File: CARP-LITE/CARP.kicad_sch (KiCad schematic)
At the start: 111 parts, among them J1 USB-C, J10 PYRO_2, J3 I2C1+3V3, J4 2S XT30, J5 UART+5V+I2C1, J6 PYRO_1, J8 PWM1+5V1, J9 PWM2+5V1, Q5 SQ2318CES, Q6 SQ2318CES, Q7 SQ2318CES, SW1 SW_Push, SW2 SW_Push, U1 W25Q128JVSIMTR (16MB), U10 TPS62130A, U2 W25Q32RVXHJQ (2MB), U3 3V3 LDO, U4 RP2350_60QFN, U5 LSM6DSO, U6 BMP390, Y1 ABM8-272-T3

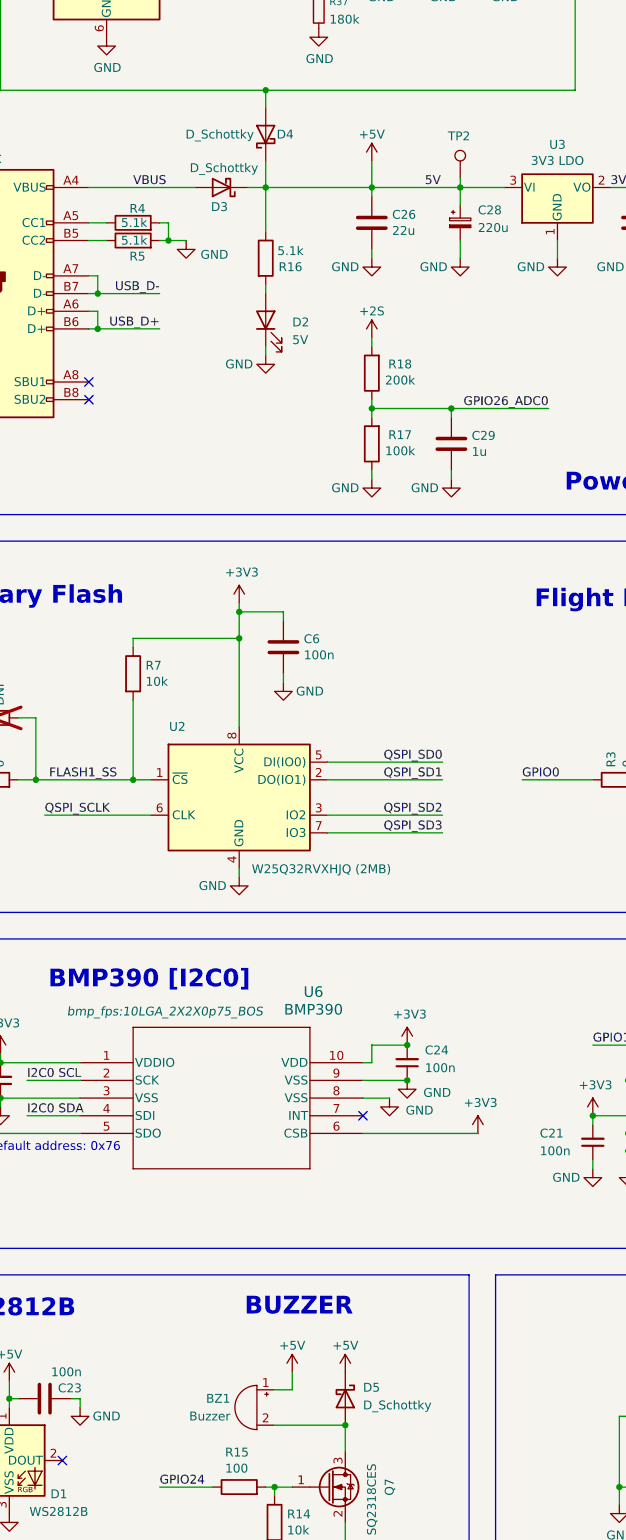
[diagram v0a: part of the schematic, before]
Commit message: Change passives footprints to 0603
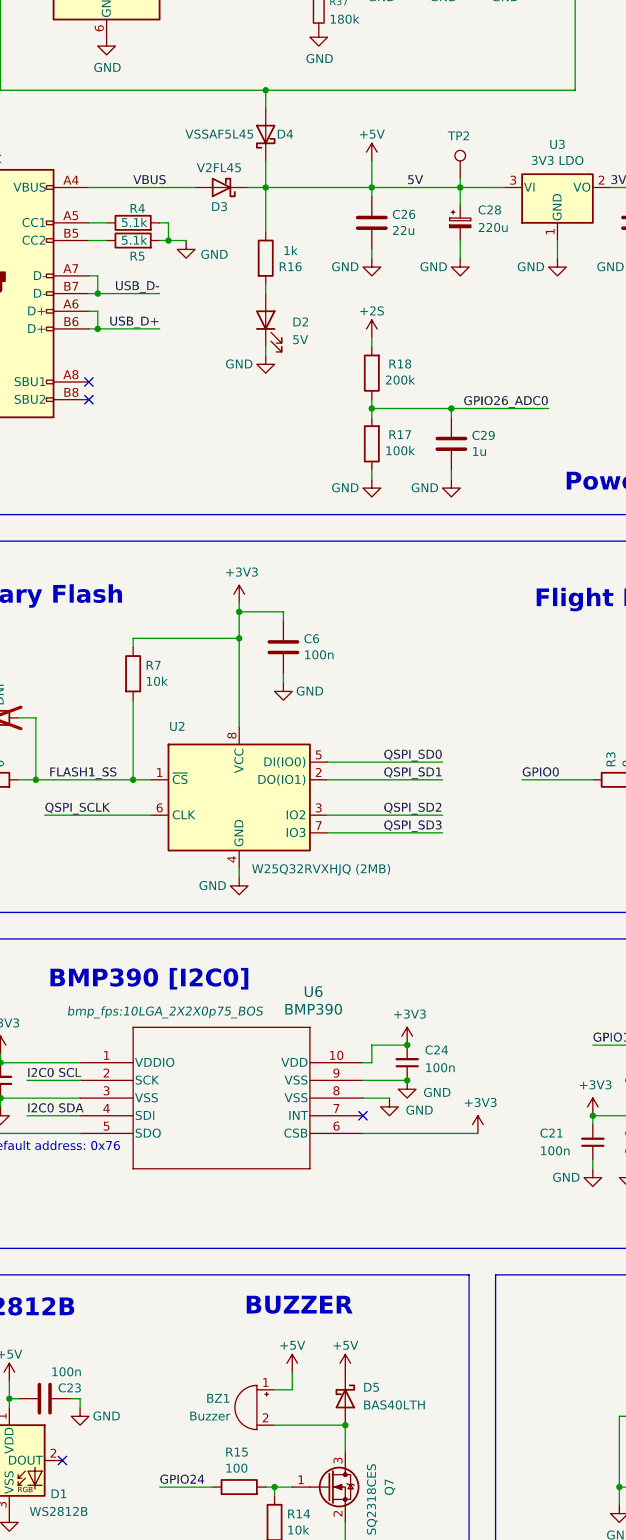
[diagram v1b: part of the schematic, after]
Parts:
- D3: value D_Schottky -> V2FL45
- D4: value D_Schottky -> VSSAF5L45
- D5: value D_Schottky -> BAS40LTH
- R16: value 5.1k -> 1k
- R19, R20, R21, R22, R24, R25, R26, R31, R32, R33, R34, R35, R4, R5, R8: footprint Resistor_SMD:R_0402_1005Metric -> Resistor_SMD:R_0603_1608Metric
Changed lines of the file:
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@@
 	)
 	(label "5V"
-		(at 93.98 81.28 0)
+		(at 91.44 81.28 0)
 		(effects
 			(font
@@
 			)
 		)
-		(property "Footprint" "Resistor_SMD:R_0402_1005Metric"
+		(property "Footprint" "Resistor_SMD:R_0603_1608Metric"
 			(at 328.93 239.268 90)
 			(hide yes)
@@
 			)
 		)
-		(property "Footprint" "Resistor_SMD:R_0402_1005Metric"
+		(property "Footprint" "Resistor_SMD:R_0603_1608Metric"
 			(at 168.148 55.88 90)
 			(hide yes)
@@
 			)
 		)
-		(property "Footprint" "Resistor_SMD:R_0402_1005Metric"
+		(property "Footprint" "Resistor_SMD:R_0603_1608Metric"
 			(at 52.07 88.138 90)
 			(hide yes)
@@
 			)
 		)
-		(property "Value" "5.1k"
+		(property "Value" "1k"
 			(at 74.676 90.3986 0)
 			(show_name no)
@@
 			)
 		)
-		(property "Footprint" "Resistor_SMD:R_0402_1005Metric"
+		(property "Footprint" "Resistor_SMD:R_0603_1608Metric"
 			(at 169.672 55.88 90)
 			(hide yes)
@@
 			)
 		)
-		(property "Footprint" "Resistor_SMD:R_0402_1005Metric"
+		(property "Footprint" "Resistor_SMD:R_0603_1608Metric"
 			(at 341.122 205.74 90)
 			(hide yes)
@@
 			)
 		)
-		(property "Value" "D_Schottky"
+		(property "Value" "BAS40LTH"
 			(at 85.09 256.2224 90)
 			(show_name no)
@@
 			)
 		)
-		(property "Footprint" "Resistor_SMD:R_0402_1005Metric"
+		(property "Footprint" "Resistor_SMD:R_0603_1608Metric"
 			(at 334.772 185.42 90)
 			(hide yes)
@@
 			)
 		)
-		(property "Footprint" "Resistor_SMD:R_0402_1005Metric"
+		(property "Footprint" "Resistor_SMD:R_0603_1608Metric"
 			(at 168.148 92.71 90)
 			(hide yes)
@@
 			)
 		)
-		(property "Footprint" "Resistor_SMD:R_0402_1005Metric"
+		(property "Footprint" "Resistor_SMD:R_0603_1608Metric"
 			(at 328.93 202.438 90)
 			(hide yes)
@@
 			)
 		)
-		(property "Footprint" "Resistor_SMD:R_0402_1005Metric"
+		(property "Footprint" "Resistor_SMD:R_0603_1608Metric"
 			(at 344.17 215.392 90)
 			(hide yes)
@@
 			)
 		)
-		(property "Footprint" "Resistor_SMD:R_0402_1005Metric"
+		(property "Footprint" "Resistor_SMD:R_0603_1608Metric"
 			(at 161.29 266.192 90)
 			(hide yes)
@@
 			)
 		)
-		(property "Footprint" "Resistor_SMD:R_0402_1005Metric"
+		(property "Footprint" "Resistor_SMD:R_0603_1608Metric"
 			(at 52.07 90.678 90)
 			(hide yes)
@@
 			)
 		)
-		(property "Footprint" "Resistor_SMD:R_0402_1005Metric"
+		(property "Footprint" "Resistor_SMD:R_0603_1608Metric"
 			(at 341.122 242.57 90)
 			(hide yes)
@@
 			)
 		)
-		(property "Footprint" "Resistor_SMD:R_0402_1005Metric"
+		(property "Footprint" "Resistor_SMD:R_0603_1608Metric"
 			(at 334.772 222.25 90)
 			(hide yes)
@@
 			)
 		)
-		(property "Footprint" "Resistor_SMD:R_0402_1005Metric"
+		(property "Footprint" "Resistor_SMD:R_0603_1608Metric"
 			(at 169.672 92.71 90)
 			(hide yes)
@@
 			)
 		)
-		(property "Footprint" "Resistor_SMD:R_0402_1005Metric"
+		(property "Footprint" "Resistor_SMD:R_0603_1608Metric"
 			(at 344.17 178.562 90)
 			(hide yes)
@@
 			)
 		)
-		(property "Value" "D_Schottky"
-			(at 60.198 78.486 0)
+		(property "Value" "V2FL45"
+			(at 61.214 78.486 0)
 			(show_name no)
 			(do_not_autoplace no)
@@
 			)
 		)
-		(property "Value" "D_Schottky"
+		(property "Value" "VSSAF5L45"
 			(at 64.516 73.66 90)
 			(show_name no)

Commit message: pcb work
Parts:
- R17, R18, R19, R20, R21, R22, R24, R25, R26, R31, R33, R34, R35, R4, R5, R8: footprint Resistor_SMD:R_0603_1608Metric -> Resistor_SMD:R_0402_1005Metric
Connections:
- net GPIO28 is gone; now on net GPIO28_ADC2: C31.2, R24.1, R26.2
- net GPIO29 is gone; now on net GPIO29_ADC3: C32.2, R32.1, R34.2
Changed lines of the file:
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@@
 		)
 	)
-	(label "GPIO28"
+	(label "GPIO28_ADC2"
 		(at 311.15 217.17 0)
 		(effects
@@
 		)
 	)
-	(label "GPIO29"
+	(label "GPIO29_ADC3"
 		(at 311.15 180.34 0)
 		(effects
@@
 			)
 		)
-		(property "Footprint" "Resistor_SMD:R_0603_1608Metric"
+		(property "Footprint" "Resistor_SMD:R_0402_1005Metric"
 			(at 328.93 239.268 90)
 			(hide yes)
@@
 			)
 		)
-		(property "Footprint" "Resistor_SMD:R_0603_1608Metric"
+		(property "Footprint" "Resistor_SMD:R_0402_1005Metric"
 			(at 168.148 55.88 90)
 			(hide yes)
@@
 			)
 		)
-		(property "Footprint" "Resistor_SMD:R_0603_1608Metric"
+		(property "Footprint" "Resistor_SMD:R_0402_1005Metric"
 			(at 52.07 88.138 90)
 			(hide yes)
@@
 			)
 		)
-		(property "Footprint" "Resistor_SMD:R_0603_1608Metric"
+		(property "Footprint" "Resistor_SMD:R_0402_1005Metric"
 			(at 169.672 55.88 90)
 			(hide yes)
@@
 			)
 		)
-		(property "Footprint" "Resistor_SMD:R_0603_1608Metric"
+		(property "Footprint" "Resistor_SMD:R_0402_1005Metric"
 			(at 341.122 205.74 90)
 			(hide yes)
@@
 			)
 		)
-		(property "Footprint" "Resistor_SMD:R_0603_1608Metric"
+		(property "Footprint" "Resistor_SMD:R_0402_1005Metric"
 			(at 168.148 92.71 90)
 			(hide yes)
@@
 			)
 		)
-		(property "Footprint" "Resistor_SMD:R_0603_1608Metric"
+		(property "Footprint" "Resistor_SMD:R_0402_1005Metric"
 			(at 328.93 202.438 90)
 			(hide yes)
@@
 			)
 		)
-		(property "Footprint" "Resistor_SMD:R_0603_1608Metric"
+		(property "Footprint" "Resistor_SMD:R_0402_1005Metric"
 			(at 344.17 215.392 90)
 			(hide yes)
@@
 			)
 		)
-		(property "Footprint" "Resistor_SMD:R_0603_1608Metric"
+		(property "Footprint" "Resistor_SMD:R_0402_1005Metric"
 			(at 161.29 266.192 90)
 			(hide yes)
@@
 			)
 		)
-		(property "Footprint" "Resistor_SMD:R_0603_1608Metric"
+		(property "Footprint" "Resistor_SMD:R_0402_1005Metric"
 			(at 88.138 107.95 90)
 			(hide yes)
@@
 			)
 		)
-		(property "Footprint" "Resistor_SMD:R_0603_1608Metric"
+		(property "Footprint" "Resistor_SMD:R_0402_1005Metric"
 			(at 88.138 118.11 90)
 			(hide yes)
@@
 			)
 		)
-		(property "Footprint" "Resistor_SMD:R_0603_1608Metric"
+		(property "Footprint" "Resistor_SMD:R_0402_1005Metric"
 			(at 52.07 90.678 90)
 			(hide yes)
@@
 			)
 		)
-		(property "Footprint" "Resistor_SMD:R_0603_1608Metric"
+		(property "Footprint" "Resistor_SMD:R_0402_1005Metric"
 			(at 341.122 242.57 90)
 			(hide yes)
@@
 			)
 		)
-		(property "Footprint" "Resistor_SMD:R_0603_1608Metric"
+		(property "Footprint" "Resistor_SMD:R_0402_1005Metric"
 			(at 334.772 222.25 90)
 			(hide yes)
@@
 			)
 		)
-		(property "Footprint" "Resistor_SMD:R_0603_1608Metric"
+		(property "Footprint" "Resistor_SMD:R_0402_1005Metric"
 			(at 169.672 92.71 90)
 			(hide yes)
@@
 			)
 		)
-		(property "Footprint" "Resistor_SMD:R_0603_1608Metric"
+		(property "Footprint" "Resistor_SMD:R_0402_1005Metric"
 			(at 344.17 178.562 90)
 			(hide yes)

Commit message: buck
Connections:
- net +5V1: now also C35.1, J8.3 (Pin_3)
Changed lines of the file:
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@@
+	(symbol
+		(lib_id "power:+5V")
+		(at 209.55 267.97 0)
+		(unit 1)
+		(body_style 1)
+		(exclude_from_sim no)
+		(in_bom yes)
+		(on_board yes)
+		(in_pos_files yes)
+		(dnp no)
+		(fields_autoplaced yes)
+		(property "Reference" "#PWR0117"
+			(at 209.55 271.78 0)
+			(hide yes)
+			(show_name no)
+			(do_not_autoplace no)
+			(effects
+				(font
+					(size 1.27 1.27)
+				)
+			)
+		)
+		(property "Value" "+5V1"
+			(at 212.09 266.6999 0)
+			(show_name no)
+			(do_not_autoplace no)
+			(effects
+				(font
+					(size 1.27 1.27)
+				)
+				(justify left)
+			)
+		)
+		(property "Footprint" ""
+			(at 209.55 267.97 0)
+			(hide yes)
+			(show_name no)
+			(do_not_autoplace no)
+			(effects
+				(font
+					(size 1.27 1.27)
+				)
+			)
+		)
+		(property "Datasheet" ""
+			(at 209.55 267.97 0)
+			(hide yes)
+			(show_name no)
+			(do_not_autoplace no)
+			(effects
+				(font
+					(size 1.27 1.27)
+				)
+			)
+		)
+		(property "Description" "Power symbol creates a global label with name \"+5V\""
+			(at 209.55 267.97 0)
+			(hide yes)
+			(show_name no)
+			(do_not_autoplace no)
+			(effects
+				(font
+					(size 1.27 1.27)
+				)
+			)
+		)
+		(pin "1"
+		)
+		(instances
+			(project "CARP"
+				(path "/94683f5c-9cd9-448e-be96-9792537b5cb8"
+					(reference "#PWR0117")
+					(unit 1)
+				)
+			)
+		)
+	)
 	(symbol
 		(lib_id "power:+5V")

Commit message: bzzzt
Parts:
- removed R28: 0, Jumper:SolderJumper-2_P1.3mm_Bridged_RoundedPad1.0x1.5mm, symbol Device:R_Small
- removed U3: 3V3 LDO, Package_TO_SOT_SMD:SOT-223-3_TabPin2, symbol Regulator_Linear:NCP1117-3.3_SOT223
- added U7: TLV75733PDBV, Package_TO_SOT_SMD:SOT-23-5, symbol Regulator_Linear:TLV75733PDBV
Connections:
- net +3V3: now also U7.5 (OUT)
- net +5V: now also U7.1 (IN), U7.3 (EN)
- net GND: now also U7.2 (GND)
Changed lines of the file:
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@@
 	)
 	(junction
+		(at 105.41 81.28)
+		(diameter 0)
+		(color 0 0 0 0)
+	)
+	(junction
 		(at 284.48 43.18)
 		(diameter 0)
@@
 	(wire
 		(pts
-			(xy 113.03 88.9) (xy 113.03 91.44)
-		)
-		(stroke
-			(width 0)
-			(type default)
-		)
-	)
-	(wire
-		(pts
 			(xy 336.55 109.22) (xy 351.79 109.22)
 		)
@@
 	(wire
 		(pts
-			(xy 358.14 144.78) (xy 374.65 144.78)
-		)
-		(stroke
-			(width 0)
-			(type default)
-		)
-	)
-	(wire
-		(pts
 			(xy 198.12 226.06) (xy 212.09 226.06)
 		)
@@
 	(wire
 		(pts
+			(xy 105.41 81.28) (xy 105.41 83.82)
+		)
+		(stroke
+			(width 0)
+			(type default)
+		)
+	)
+	(wire
+		(pts
 			(xy 209.55 271.78) (xy 210.82 271.78)
 		)
@@
 		)
 	)
-	(label "GPIO27_ADC1"
-		(at 374.65 144.78 180)
-		(effects
-			(font
-				(size 1.27 1.27)
-			)
-			(justify right bottom)
-		)
-	)
 	(label "GPIO12"
 		(at 238.76 270.51 0)
@@
 	)
 	(symbol
-		(lib_id "Regulator_Linear:NCP1117-3.3_SOT223")
-		(at 113.03 81.28 0)
-		(unit 1)
-		(body_style 1)
-		(exclude_from_sim no)
-		(in_bom yes)
-		(on_board yes)
-		(in_pos_files yes)
-		(dnp no)
-		(property "Reference" "U3"
-			(at 113.03 75.1332 0)
-			(show_name no)
-			(do_not_autoplace no)
-			(effects
-				(font
-					(size 1.27 1.27)
-				)
-			)
-		)
-		(property "Value" "3V3 LDO"
-			(at 113.03 77.4446 0)
-			(show_name no)
-			(do_not_autoplace no)
-			(effects
-				(font
-					(size 1.27 1.27)
-				)
-			)
-		)
-		(property "Footprint" "Package_TO_SOT_SMD:SOT-223-3_TabPin2"
-			(at 113.03 76.2 0)
-			(hide yes)
-			(show_name no)
-			(do_not_autoplace no)
-			(effects
-				(font
-					(size 1.27 1.27)
-				)
-			)
-		)
-		(property "Datasheet" "http://www.onsemi.com/pub_link/Collateral/NCP1117-D.PDF"
-			(at 115.57 87.63 0)
-			(hide yes)
-			(show_name no)
-			(do_not_autoplace no)
-			(effects
-				(font
-					(size 1.27 1.27)
-				)
-			)
-		)
-		(property "Description" ""
-			(at 113.03 81.28 0)
-			(show_name no)
-			(do_not_autoplace no)
-			(effects
-				(font
-					(size 1.27 1.27)
-				)
-			)
-		)
-		(pin "1"
-		)
-		(pin "2"
-		)
-		(pin "3"
-		)
-		(instances
-			(project "CARP"
-				(path "/94683f5c-9cd9-448e-be96-9792537b5cb8"
-					(reference "U3")
-					(unit 1)
-				)
-			)
-		)
-	)
-	(symbol
 		(lib_id "power:GND")
 		(at 113.03 91.44 0)
@@
 	)
 	(symbol
+		(lib_id "Regulator_Linear:TLV75733PDBV")
+		(at 113.03 83.82 0)
+		(unit 1)
+		(body_style 1)
+		(exclude_from_sim no)
+		(in_bom yes)
+		(on_board yes)
+		(in_pos_files yes)
+		(dnp no)
+		(fields_autoplaced yes)
+		(property "Reference" "U7"
+			(at 113.03 74.93 0)
+			(show_name no)
+			(do_not_autoplace no)
+			(effects
+				(font
+					(size 1.27 1.27)
+				)
+			)
+		)
+		(property "Value" "TLV75733PDBV"
+			(at 113.03 77.47 0)
+			(show_name no)
+			(do_not_autoplace no)
+			(effects
+				(font
+					(size 1.27 1.27)
+				)
+			)
+		)
+		(property "Footprint" "Package_TO_SOT_SMD:SOT-23-5"
+			(at 113.03 75.565 0)
+			(hide yes)
+			(show_name no)
+			(do_not_autoplace no)
+			(effects
+				(font
+					(size 1.27 1.27)
+					(italic yes)
+				)
+			)
+		)
+		(property "Datasheet" "https://www.ti.com/lit/ds/symlink/tlv757p.pdf"
+			(at 113.03 82.55 0)
+			(hide yes)
+			(show_name no)
+			(do_not_autoplace no)
+			(effects
+				(font
+					(size 1.27 1.27)
+				)
+			)
+		)
+		(property "Description" "1A Low IQ Small Size Low Dropout Voltage Regulator, Fixed Output 3.3V, SOT-23-5"
+			(at 113.03 83.82 0)
+			(hide yes)
+			(show_name no)
+			(do_not_autoplace no)
+			(effects
+				(font
+					(size 1.27 1.27)
+				)
+			)
+		)
+		(pin "3"
+		)
+		(pin "5"
+		)
+		(pin "1"
+		)
+		(pin "2"
+		)
+		(pin "4"
+		)
+		(instances
+			(project "CARP"
+				(path "/94683f5c-9cd9-448e-be96-9792537b5cb8"
+					(reference "U7")
+					(unit 1)
+				)
+			)
+		)
+	)
+	(symbol
 		(lib_id "Device:R")
 		(at 139.7 151.13 0)
@@
 					(unit 1)
 				)
-			)
-		)
-	)
-	(symbol
-		(lib_id "Device:R_Small")
-		(at 355.6 144.78 90)
-		(unit 1)
-		(body_style 1)
-		(exclude_from_sim no)
-		(in_bom yes)
-		(on_board yes)
-		(in_pos_files yes)
-		(dnp no)
-		(property "Reference" "R28"
-			(at 352.298 144.018 90)
-			(show_name no)
-			(do_not_autoplace no)
-			(effects
-				(font
-					(size 1.016 1.016)
-				)
-			)
-		)
-		(property "Value" "0"
-			(at 355.6 144.78 90)
-			(show_name no)
-			(do_not_autoplace no)
-			(effects
-				(font
-					(size 1.27 1.27)
-				)
-			)
-		)
-		(property "Footprint" "Jumper:SolderJumper-2_P1.3mm_Bridged_RoundedPad1.0x1.5mm"
-			(at 355.6 144.78 0)
-			(hide yes)
-			(show_name no)
-			(do_not_autoplace no)
-			(effects
-				(font
-					(size 1.27 1.27)
-				)
-			)
-		)
-		(property "Datasheet" ""
-			(at 355.6 144.78 0)
-			(hide yes)
-			(show_name no)
-			(do_not_autoplace no)
-			(effects
-				(font
-					(size 1.27 1.27)
-				)
-			)
-		)
-		(property "Description" "Resistor, small symbol"
-			(at 355.6 144.78 0)
-			(hide yes)
-			(show_name no)
-			(do_not_autoplace no)
-			(effects
-				(font
-					(size 1.27 1.27)
-				)
-			)
-		)
-		(pin "2"
-		)
-		(pin "1"
-		)
-		(instances
-			(project "CARP"
-				(path "/94683f5c-9cd9-448e-be96-9792537b5cb8"
-					(reference "R28")
-					(unit 1)
-				)

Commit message: buck and ldo
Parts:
- C35, C63: value 220u -> 100u; footprint Capacitor_Tantalum_SMD:CP_EIA-7343-31_Kemet-D -> Capacitor_Tantalum_SMD:CP_EIA-6032-28_Kemet-C; MFR TR3D227K010C0150 -> TR3C107K010C0100
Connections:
- net PWM1 is gone; now on net GPIO23: J8.2 (Pin_2)
- net PWM2 is gone; now on net GPIO20: J9.2 (Pin_2)
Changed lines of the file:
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@@
 		)
 	)
+	(label "GPIO20"
+		(at 198.12 254 0)
+		(effects
+			(font
+				(size 1.27 1.27)
+			)
+			(justify left bottom)
+		)
+	)
 	(label "QSPI_SD2"
 		(at 96.52 171.45 180)
@@
 		)
 	)
-	(label "PWM2"
-		(at 198.12 254 0)
-		(effects
-			(font
-				(size 1.27 1.27)
-			)
-			(justify left bottom)
-		)
-	)
 	(label "QSPI_SD0"
 		(at 259.08 88.9 0)
@@
 		)
 	)
+	(label "GPIO23"
+		(at 198.12 274.32 0)
+		(effects
+			(font
+				(size 1.27 1.27)
+			)
+			(justify left bottom)
+		)
+	)
 	(label "GPIO24"
 		(at 55.88 267.97 0)
@@
 		)
 	)
-	(label "PWM1"
-		(at 198.12 274.32 0)
-		(effects
-			(font
-				(size 1.27 1.27)
-			)
-			(justify left bottom)
-		)
-	)
 	(label "USB_D-"
 		(at 365.76 66.04 180)
@@
 			)
 		)
-		(property "Value" "220u"
+		(property "Value" "100u"
 			(at 203.7461 265.43 90)
 			(show_name no)
@@
 			)
 		)
-		(property "Footprint" "Capacitor_Tantalum_SMD:CP_EIA-7343-31_Kemet-D"
+		(property "Footprint" "Capacitor_Tantalum_SMD:CP_EIA-6032-28_Kemet-C"
 			(at 203.2 269.24 0)
 			(hide yes)
@@
 			)
 		)
-		(property "MFR" "TR3D227K010C0150"
+		(property "MFR" "TR3C107K010C0100"
 			(at 203.2 269.24 0)
 			(hide yes)
@@
 			)
 		)
-		(property "Value" "220u"
+		(property "Value" "100u"
 			(at 203.7461 245.11 90)
 			(show_name no)
@@
 			)
 		)
-		(property "Footprint" "Capacitor_Tantalum_SMD:CP_EIA-7343-31_Kemet-D"
+		(property "Footprint" "Capacitor_Tantalum_SMD:CP_EIA-6032-28_Kemet-C"
 			(at 203.2 248.92 0)
 			(hide yes)
@@
 			)
 		)
-		(property "MFR" "TR3D227K010C0150"
+		(property "MFR" "TR3C107K010C0100"
 			(at 203.2 248.92 0)
 			(hide yes)

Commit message: łełołeło
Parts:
- R32: footprint Resistor_SMD:R_0603_1608Metric -> Resistor_SMD:R_0402_1005Metric
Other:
- note removed: "##### TODO ##### choose and optimize footprints: - main cap (move from servo out to 2S ?) - buzzer ponder servo power keep slaving away at the pcb"
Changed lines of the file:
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@@
 		)
 	)
-	(text "##### TODO #####\n\nchoose and optimize footprints:\n- main cap (move from servo out to 2S ?)\n- buzzer\n\nponder servo power\n\nkeep slaving away at the pcb"
-		(exclude_from_sim no)
-		(at 194.818 184.658 0)
-		(effects
-			(font
-				(size 1.27 1.27)
-				(thickness 0.254)
-				(bold yes)
-			)
-			(justify left)
-		)
-	)
 	(text "BMP390 HIGH SPEED"
 		(exclude_from_sim no)
@@
 			)
 		)
-		(property "Footprint" "Resistor_SMD:R_0603_1608Metric"
+		(property "Footprint" "Resistor_SMD:R_0402_1005Metric"
 			(at 334.772 185.42 90)
 			(hide yes)
